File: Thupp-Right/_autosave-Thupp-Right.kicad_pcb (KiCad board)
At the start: 2 copper layers, 42 parts

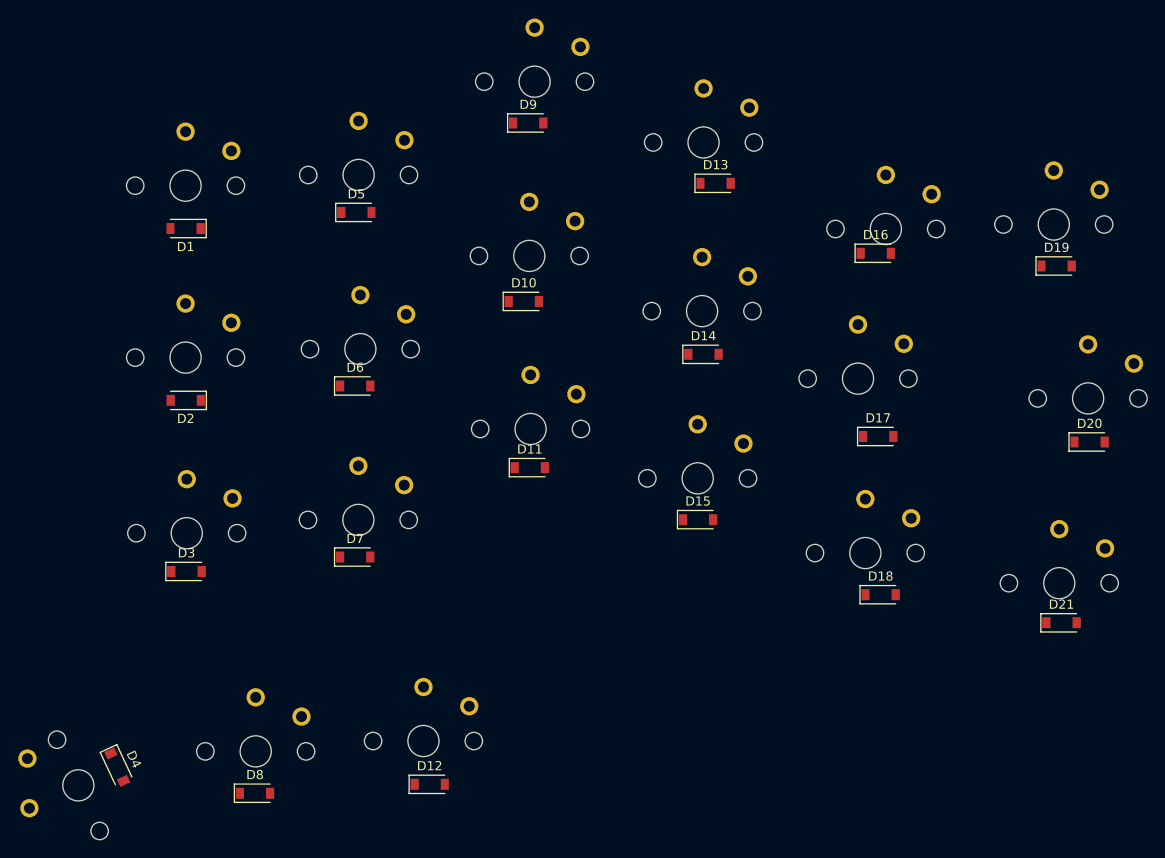
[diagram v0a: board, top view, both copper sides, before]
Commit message: added crides footprint with diode
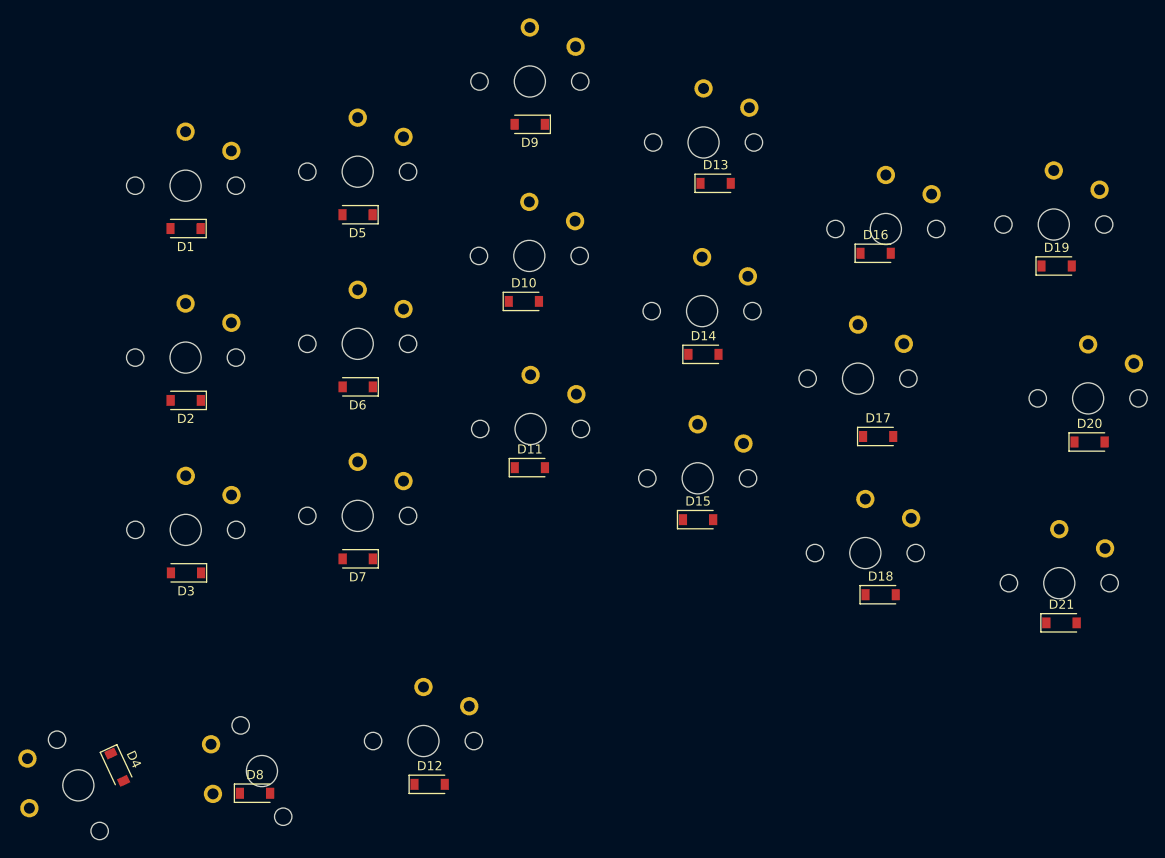
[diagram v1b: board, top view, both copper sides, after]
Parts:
- moved MX8 2.25 mm to (56.2, 104.5), turned to 115 degrees
- moved MX6 0.65 mm to (66.7, 57.9)
- moved MX9 0.52 mm to (85.5, 29.2)
- moved MX7 0.45 mm to (66.7, 76.7)
- moved MX3 0.38 mm to (47.9, 78.2)
- moved MX5 0.37 mm to (66.7, 39.1)
- moved D7 0.34 mm to (66.7, 81.3), turned to 180 degrees
- moved D6 0.30 mm to (66.7, 62.6), turned to 180 degrees
- moved D5 0.28 mm to (66.7, 43.8), turned to 180 degrees
- moved D9 0.23 mm to (85.5, 33.9), turned to 180 degrees
- moved D3 0.16 mm to (47.9, 82.9), turned to 180 degrees
